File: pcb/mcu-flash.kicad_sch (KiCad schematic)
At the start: 25 parts, among them J1 Programming Header, SW1 SW_Push, U1 W25Q128JVS, U2 RP2040, Y1 ABM8AIG-12.000MHZ-12-2Z-T3

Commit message: Replaced through-hole components with SMD
- Other small edits (e.g. optional jumper to force USB-boot)
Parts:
- removed J1: Programming Header, symbol Connector_Generic:Conn_02x03_Odd_Even
- added J1: 0015910100, Connector_PinHeader_2.54mm:PinHeader_2x05_P2.54mm_Vertical_SMD, symbol Connector_Generic:Conn_02x05_Odd_Even
- added JP1: TSM-102-01-L-SV, Connector_PinHeader_2.54mm:PinHeader_1x02_P2.54mm_Vertical_SMD_Pin1Left, symbol Jumper:Jumper_2_Open
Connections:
- net +3.3V: now also J1.1 (Pin_1), J1.3 (Pin_3)
- net GND: now also J1.10 (Pin_10), J1.5 (Pin_5), J1.7 (Pin_7), J1.8 (Pin_8), J1.9 (Pin_9), JP1.1 (A)
- net QSPI_{CLK}: now also JP1.2 (B)
- net ~{RESET}: now also J1.6 (Pin_6)
- net at U2.25 (SWD): now also J1.4 (Pin_4)
- net at U2.24 (SWCLK): now also J1.2 (Pin_2)
- no-connect marks 15 -> 14
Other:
- company: (none) -> Open Ephys, Inc.
- title: (none) -> Open Ephys Commutator Controller

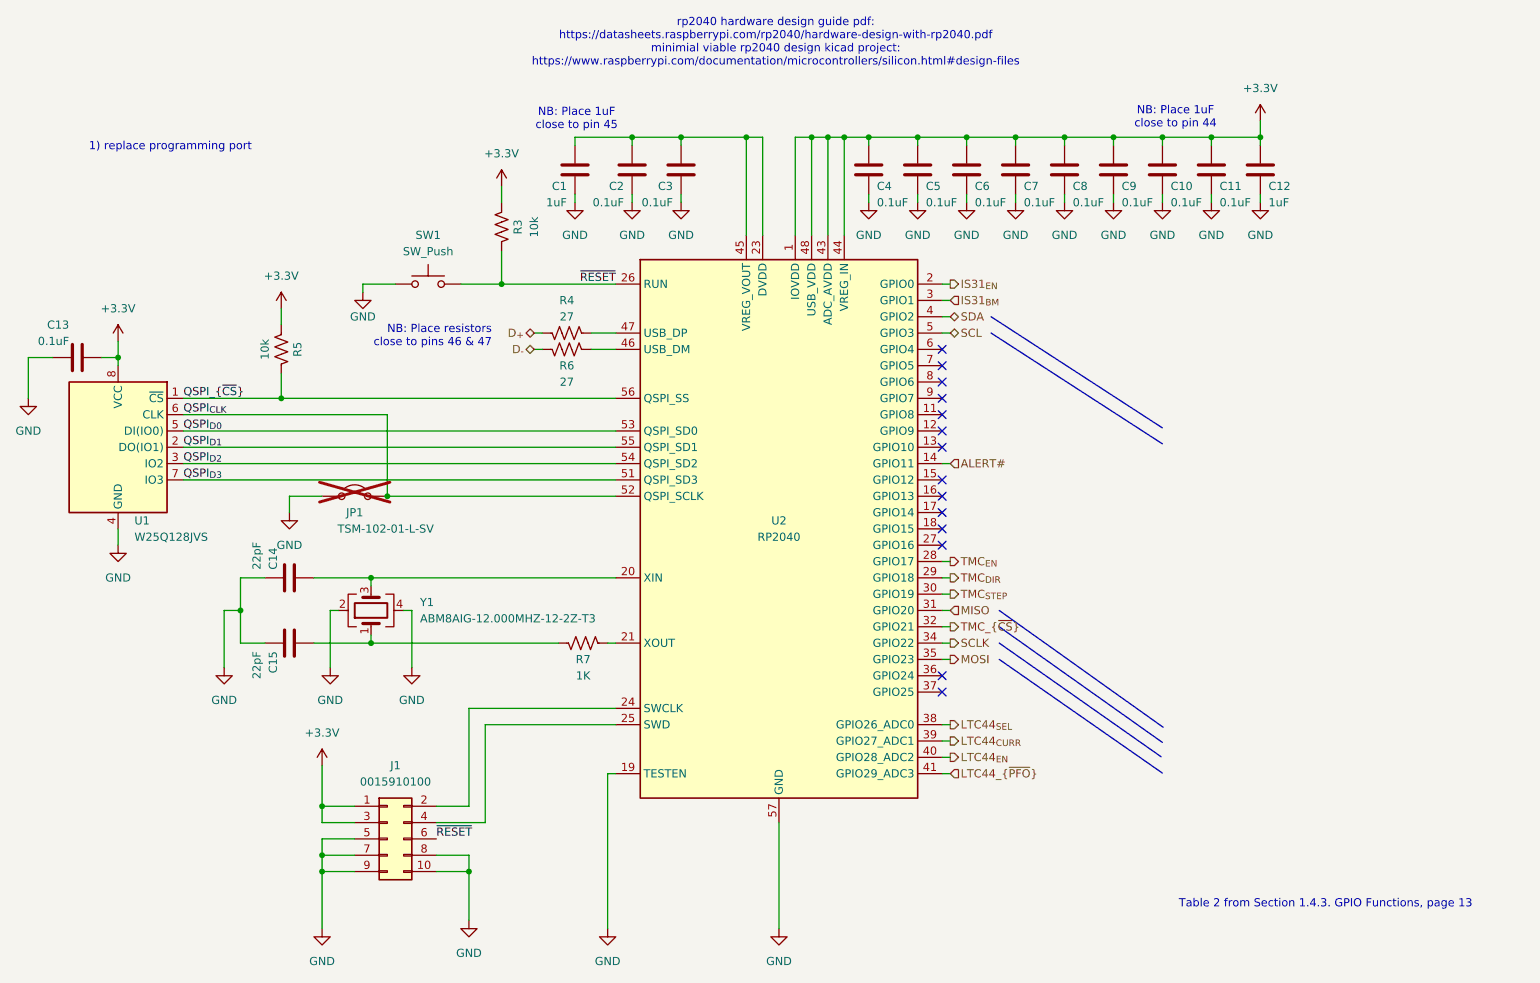
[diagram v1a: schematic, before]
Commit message: Add GPIO to programming header
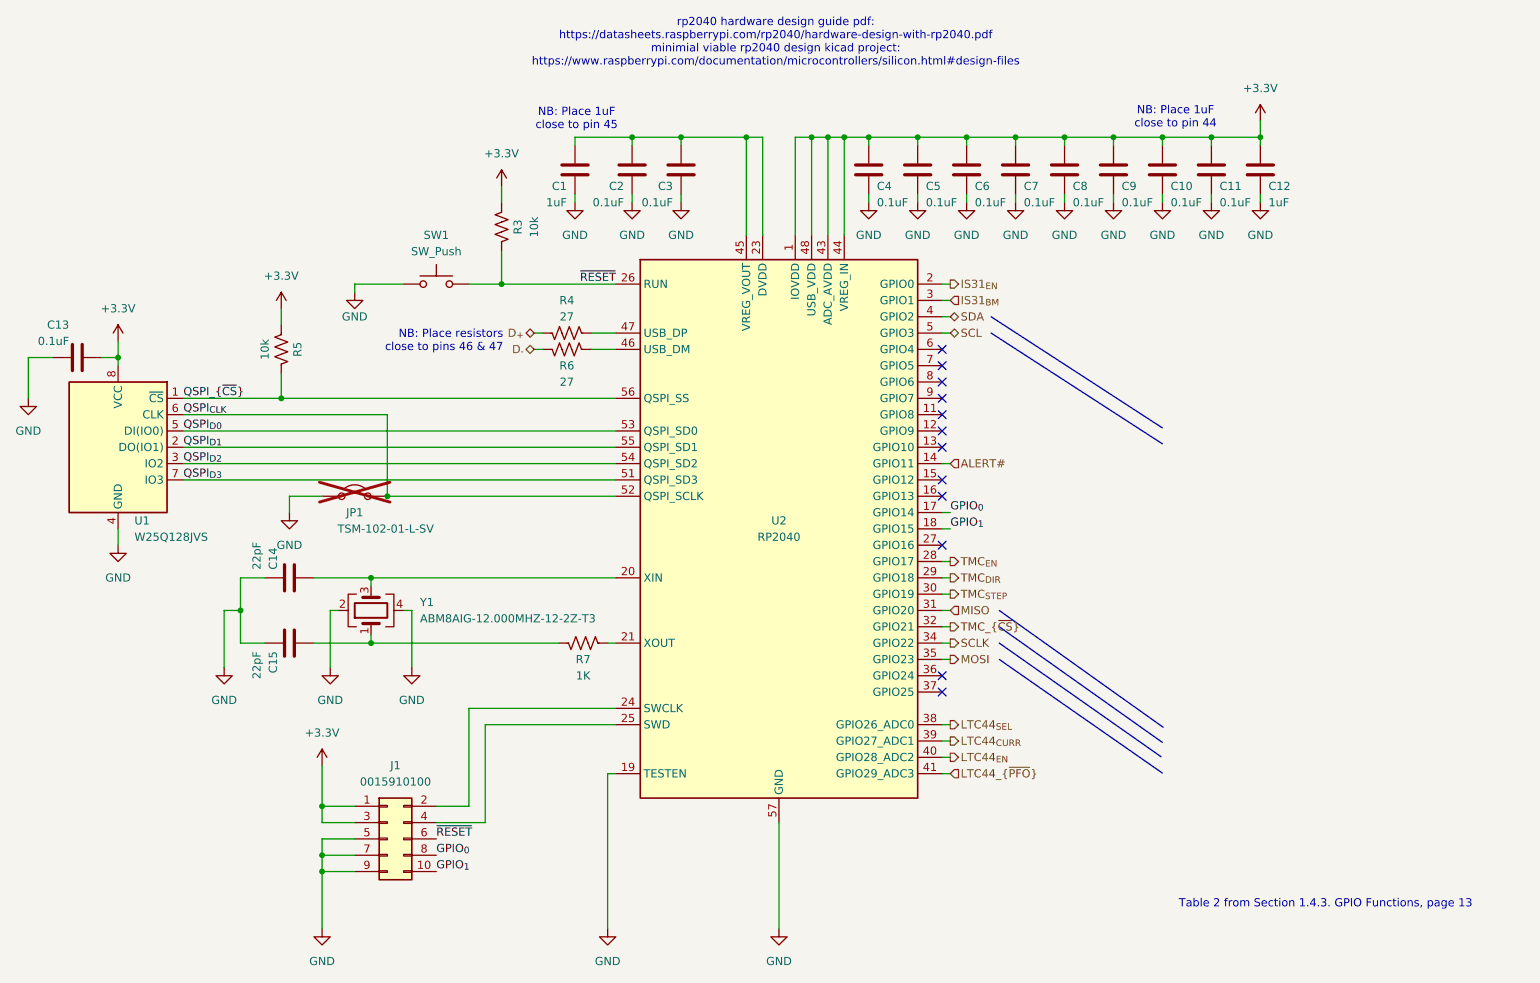
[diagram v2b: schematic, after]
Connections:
- net GND: no longer J1.10 (Pin_10), J1.8 (Pin_8)
- net GPIO_{0}: now reaches U2.17 (GPIO14)
- net GPIO_{0}: now also J1.8 (Pin_8)
- net GPIO_{1}: now reaches U2.18 (GPIO15)
- net GPIO_{1}: now also J1.10 (Pin_10)
- no-connect marks 14 -> 12
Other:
- note removed: "1) replace programming port"
- moved on the sheet: SW1
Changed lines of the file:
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@@
 	)
 	(junction
-		(at 93.98 154.94)
-		(diameter 0)
-		(color 0 0 0 0)
-	)
-	(junction
 		(at 152.4 40.64)
 		(diameter 0)
@@
 	)
 	(no_connect
-		(at 167.64 73.66)
+		(at 167.64 124.46)
 	)
 	(no_connect
-		(at 167.64 99.06)
+		(at 167.64 73.66)
 	)
 	(no_connect
@@
 	)
 	(no_connect
-		(at 167.64 127)
+		(at 167.64 86.36)
 	)
 	(no_connect
-		(at 167.64 86.36)
+		(at 167.64 127)
 	)
 	(no_connect
@@
 	)
 	(no_connect
-		(at 167.64 101.6)
-	)
-	(no_connect
 		(at 167.64 76.2)
 	)
@@
 	)
 	(no_connect
-		(at 167.64 124.46)
-	)
-	(no_connect
 		(at 167.64 83.82)
 	)
@@
 	(wire
 		(pts
+			(xy 168.91 99.06) (xy 167.64 99.06)
+		)
+		(stroke
+			(width 0)
+			(type default)
+		)
+	)
+	(wire
+		(pts
 			(xy 209.55 41.91) (xy 209.55 40.64)
 		)
@@
 	(wire
 		(pts
-			(xy 93.98 152.4) (xy 88.9 152.4)
-		)
-		(stroke
-			(width 0)
-			(type default)
-		)
-	)
-	(wire
-		(pts
 			(xy 168.91 119.38) (xy 167.64 119.38)
 		)
@@
 	(wire
 		(pts
-			(xy 88.9 154.94) (xy 93.98 154.94)
-		)
-		(stroke
-			(width 0)
-			(type default)
-		)
-	)
-	(wire
-		(pts
 			(xy 49.53 88.9) (xy 116.84 88.9)
 		)
@@
 	(wire
 		(pts
-			(xy 92.71 63.5) (xy 99.06 63.5)
+			(xy 93.98 63.5) (xy 99.06 63.5)
 		)
 		(stroke
@@
 	(wire
 		(pts
-			(xy 77.47 63.5) (xy 77.47 64.77)
+			(xy 76.2 63.5) (xy 76.2 64.77)
 		)
 		(stroke
@@
 	(wire
 		(pts
-			(xy 93.98 154.94) (xy 93.98 162.56)
-		)
-		(stroke
-			(width 0)
-			(type default)
-		)
-	)
-	(wire
-		(pts
 			(xy 147.32 40.64) (xy 147.32 55.88)
 		)
@@
 	(wire
 		(pts
-			(xy 93.98 152.4) (xy 93.98 154.94)
-		)
-		(stroke
-			(width 0)
-			(type default)
-		)
-	)
-	(wire
-		(pts
 			(xy 163.83 40.64) (xy 171.45 40.64)
 		)
@@
 	(wire
 		(pts
-			(xy 77.47 63.5) (xy 82.55 63.5)
+			(xy 76.2 63.5) (xy 83.82 63.5)
 		)
 		(stroke
@@
 	(wire
 		(pts
+			(xy 168.91 101.6) (xy 167.64 101.6)
+		)
+		(stroke
+			(width 0)
+			(type default)
+		)
+	)
+	(wire
+		(pts
 			(xy 163.83 41.91) (xy 163.83 40.64)
 		)
@@
 	(text "NB: Place resistors\nclose to pins 46 & 47"
 		(exclude_from_sim no)
-		(at 97.536 73.406 0)
+		(at 99.314 74.168 0)
 		(effects
 			(font
@@
 		)
 	)
-	(text "1) replace programming port\n"
-		(exclude_from_sim no)
-		(at 47.498 42.164 0)
-		(effects
-			(font
-				(size 1.27 1.27)
-			)
-		)
-	)
 	(text "Table 2 from Section 1.4.3. GPIO Functions, page 13"
 		(exclude_from_sim no)
@@
 		)
 	)
+	(label "GPIO_{0}"
+		(at 168.91 99.06 0)
+		(fields_autoplaced yes)
+		(effects
+			(font
+				(size 1.27 1.27)
+			)
+			(justify left bottom)
+		)
+	)
 	(label "QSPI_{D3}"
 		(at 49.53 93.98 0)
@@
 		)
 	)
+	(label "GPIO_{1}"
+		(at 88.9 154.94 0)
+		(fields_autoplaced yes)
+		(effects
+			(font
+				(size 1.27 1.27)
+			)
+			(justify left bottom)
+		)
+	)
+	(label "GPIO_{1}"
+		(at 168.91 101.6 0)
+		(fields_autoplaced yes)
+		(effects
+			(font
+				(size 1.27 1.27)
+			)
+			(justify left bottom)
+		)
+	)
+	(label "GPIO_{0}"
+		(at 88.9 152.4 0)
+		(fields_autoplaced yes)
+		(effects
+			(font
+				(size 1.27 1.27)
+			)
+			(justify left bottom)
+		)
+	)
 	(label "QSPI_{~{CS}}"
 		(at 49.53 81.28 0)
@@
 	(symbol
 		(lib_id "power:GND")
-		(at 77.47 64.77 0)
+		(at 76.2 64.77 0)
 		(unit 1)
 		(exclude_from_sim no)
@@
 		(dnp no)
 		(property "Reference" "#PWR016"
-			(at 77.47 71.12 0)
+			(at 76.2 71.12 0)
 			(effects
 				(font
@@
 		)
 		(property "Value" "GND"
-			(at 77.47 68.58 0)
+			(at 76.2 68.58 0)
 			(effects
 				(font
@@
 		)
 		(property "Footprint" ""
-			(at 77.47 64.77 0)
+			(at 76.2 64.77 0)
 			(effects
 				(font
@@
 		)
 		(property "Datasheet" ""
-			(at 77.47 64.77 0)
+			(at 76.2 64.77 0)
 			(effects
 				(font
@@
 		)
 		(property "Description" "Power symbol creates a global label with name \"GND\" , ground"
-			(at 77.47 64.77 0)
+			(at 76.2 64.77 0)
 			(effects
 				(font
@@
 	(symbol
 		(lib_id "power:GND")
-		(at 93.98 162.56 0)
-		(mirror y)
-		(unit 1)
-		(exclude_from_sim no)
-		(in_bom yes)
-		(on_board yes)
-		(dnp no)
-		(fields_autoplaced yes)
-		(property "Reference" "#PWR077"
-			(at 93.98 168.91 0)
-			(effects
-				(font
-					(size 1.27 1.27)
-				)
-				(hide yes)
-			)
-		)
-		(property "Value" "GND"
-			(at 93.98 167.64 0)
-			(effects
-				(font
-					(size 1.27 1.27)
-				)
-			)
-		)
-		(property "Footprint" ""
-			(at 93.98 162.56 0)
-			(effects
-				(font
-					(size 1.27 1.27)
-				)
-				(hide yes)
-			)
-		)
-		(property "Datasheet" ""
-			(at 93.98 162.56 0)
-			(effects
-				(font
-					(size 1.27 1.27)
-				)
-				(hide yes)
-			)
-		)
-		(property "Description" "Power symbol creates a global label with name \"GND\" , ground"
-			(at 93.98 162.56 0)
-			(effects
-				(font
-					(size 1.27 1.27)
-				)
-				(hide yes)
-			)
-		)
-		(pin "1"
-		)
-		(instances
-			(project "oe-commutator-controller"
-				(path "/f8e1d654-dc44-4fb2-953c-f5982945ff40/f332ab09-c494-4f8f-98bf-7facb28de9af"
-					(reference "#PWR077")
-					(unit 1)
-				)
-			)
-		)
-	)
-	(symbol
-		(lib_id "power:GND")
 		(at 115.57 163.83 0)
 		(mirror y)
@@
 		)
 		(instances
-			(project ""
+			(project "oe-commutator-controller"
 				(path "/f8e1d654-dc44-4fb2-953c-f5982945ff40/f332ab09-c494-4f8f-98bf-7facb28de9af"
 					(reference "JP1")
@@
 		)
 		(instances
-			(project ""
+			(project "oe-commutator-controller"
 				(path "/f8e1d654-dc44-4fb2-953c-f5982945ff40/f332ab09-c494-4f8f-98bf-7facb28de9af"
 					(reference "J1")
@@
 	(symbol
 		(lib_id "Switch:SW_Push")
-		(at 87.63 63.5 0)
+		(at 88.9 63.5 0)
 		(unit 1)
 		(exclude_from_sim no)
@@
 		(fields_autoplaced yes)
 		(property "Reference" "SW1"
-			(at 87.63 55.88 0)
+			(at 88.9 55.88 0)
 			(effects
 				(font
@@
 		)
 		(property "Value" "SW_Push"
-			(at 87.63 58.42 0)
+			(at 88.9 58.42 0)
 			(effects
 				(font
@@
 		)
 		(property "Footprint" "Button_Switch_SMD:SW_Push_1P1T_NO_CK_KMR2"
-			(at 87.63 58.42 0)
+			(at 88.9 58.42 0)
 			(effects
 				(font
@@
 		)
 		(property "Datasheet" "https://www.ckswitches.com/media/1479/kmr2.pdf"
-			(at 87.63 58.42 0)
+			(at 88.9 58.42 0)
 			(effects
 				(font
@@
 		)
 		(property "Description" "Push button switch, generic, two pins"
-			(at 87.63 63.5 0)
+			(at 88.9 63.5 0)
 			(effects
 				(font

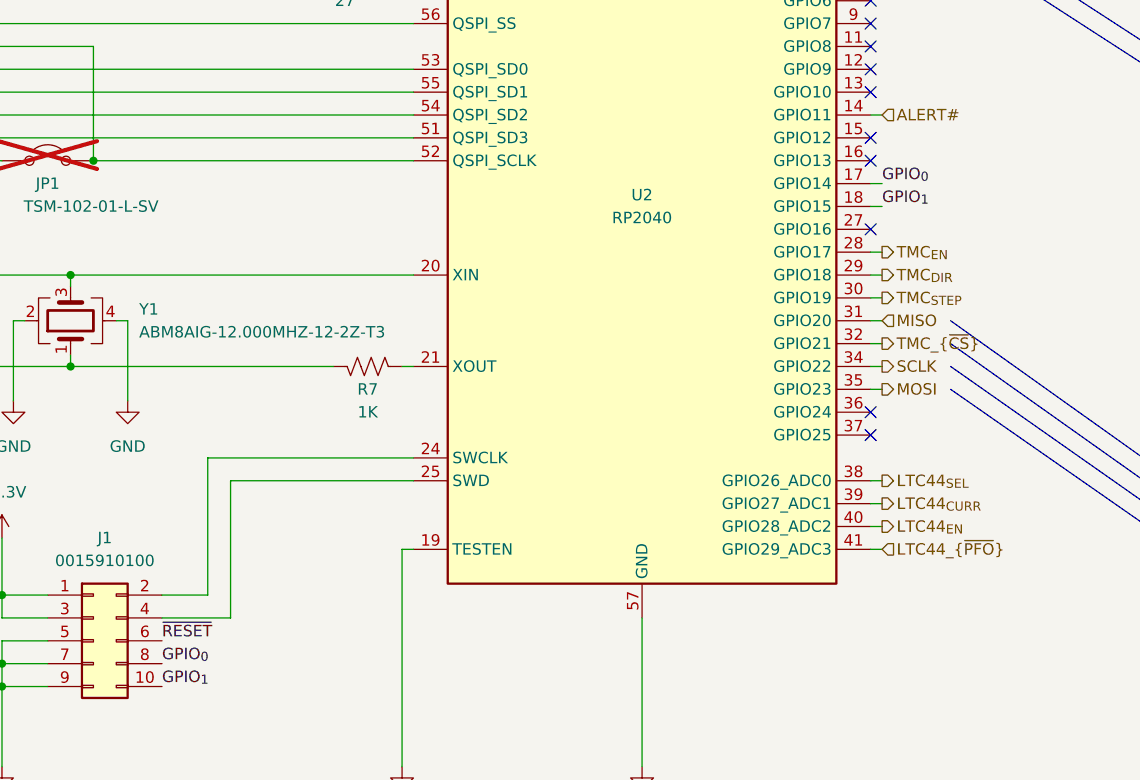
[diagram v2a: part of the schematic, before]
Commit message: Rev D PCB WIP for Review
- Before going into further minutiae, get review
- Components are laid out and routed
- Fails DRC check, requires vias for better GND plane, there are traces
  in the outer keepout zone, remove S5?
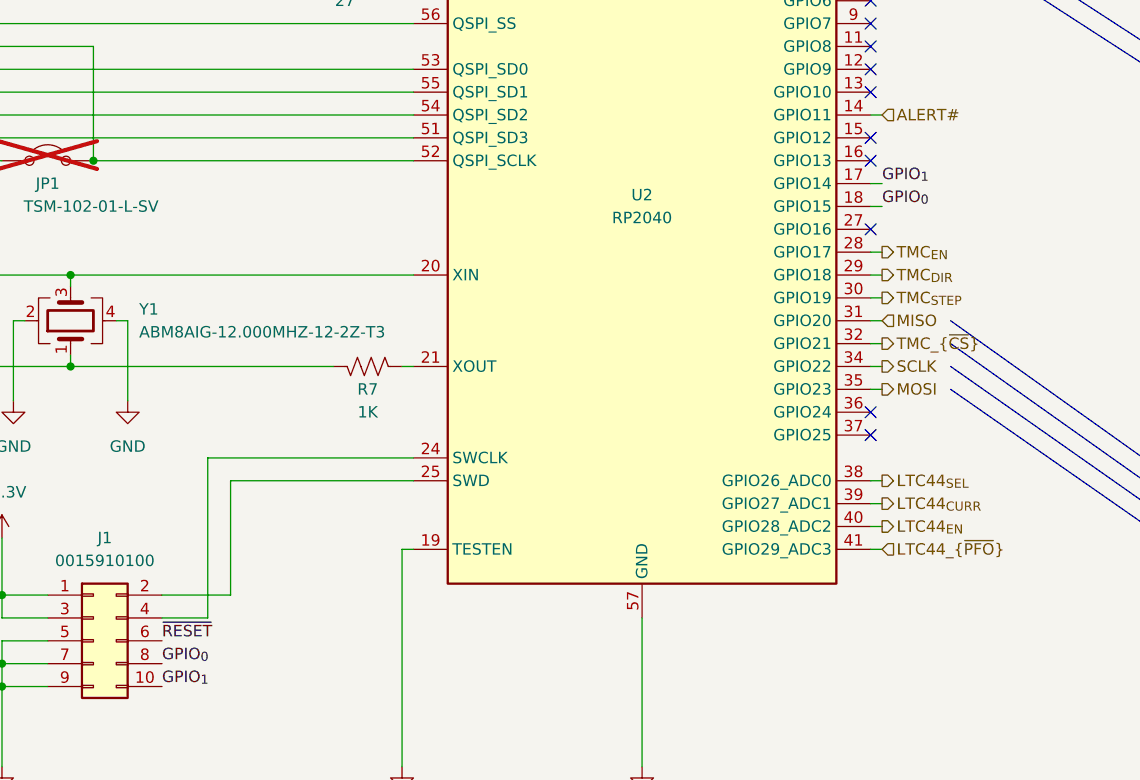
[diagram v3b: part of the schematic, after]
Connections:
- net GPIO_{0}: now also U2.18 (GPIO15); no longer U2.17 (GPIO14)
- net GPIO_{1}: now also U2.17 (GPIO14); no longer U2.18 (GPIO15)
- net at U2.24 (SWCLK): now also J1.4 (Pin_4); no longer J1.2 (Pin_2)
- net at U2.25 (SWD): now also J1.2 (Pin_2); no longer J1.4 (Pin_4)
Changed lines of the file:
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@@
 	(wire
 		(pts
-			(xy 88.9 144.78) (xy 93.98 144.78)
-		)
-		(stroke
-			(width 0)
-			(type default)
-		)
-	)
-	(wire
-		(pts
 			(xy 163.83 49.53) (xy 163.83 50.8)
 		)
@@
 	(wire
 		(pts
+			(xy 93.98 147.32) (xy 93.98 129.54)
+		)
+		(stroke
+			(width 0)
+			(type default)
+		)
+	)
+	(wire
+		(pts
 			(xy 39.37 72.39) (xy 39.37 74.93)
 		)
@@
 	(wire
 		(pts
-			(xy 96.52 132.08) (xy 96.52 147.32)
+			(xy 96.52 132.08) (xy 96.52 144.78)
 		)
 		(stroke
@@
 	(wire
 		(pts
+			(xy 88.9 144.78) (xy 96.52 144.78)
+		)
+		(stroke
+			(width 0)
+			(type default)
+		)
+	)
+	(wire
+		(pts
 			(xy 105.41 71.12) (xy 104.14 71.12)
 		)
@@
 	(wire
 		(pts
+			(xy 88.9 147.32) (xy 93.98 147.32)
+		)
+		(stroke
+			(width 0)
+			(type default)
+		)
+	)
+	(wire
+		(pts
 			(xy 168.91 116.84) (xy 167.64 116.84)
 		)
@@
 	(wire
 		(pts
-			(xy 93.98 144.78) (xy 93.98 129.54)
-		)
-		(stroke
-			(width 0)
-			(type default)
-		)
-	)
-	(wire
-		(pts
-			(xy 96.52 147.32) (xy 88.9 147.32)
-		)
-		(stroke
-			(width 0)
-			(type default)
-		)
-	)
-	(wire
-		(pts
 			(xy 115.57 119.38) (xy 116.84 119.38)
 		)
@@
 		)
 	)
-	(label "QSPI_{D1}"
-		(at 49.53 88.9 0)
+	(label "GPIO_{0}"
+		(at 168.91 101.6 0)
 		(fields_autoplaced yes)
 		(effects
@@
 		)
 	)
-	(label "GPIO_{0}"
-		(at 168.91 99.06 0)
+	(label "QSPI_{D1}"
+		(at 49.53 88.9 0)
 		(fields_autoplaced yes)
 		(effects
@@
 		)
 	)
-	(label "~{RESET}"
-		(at 116.84 63.5 180)
+	(label "GPIO_{1}"
+		(at 168.91 99.06 0)
 		(fields_autoplaced yes)
 		(effects
@@
 				(size 1.27 1.27)
 			)
-			(justify right bottom)
+			(justify left bottom)
 		)
 	)
-	(label "GPIO_{1}"
-		(at 88.9 154.94 0)
+	(label "~{RESET}"
+		(at 116.84 63.5 180)
 		(fields_autoplaced yes)
 		(effects
@@
 				(size 1.27 1.27)
 			)
-			(justify left bottom)
+			(justify right bottom)
 		)
 	)
 	(label "GPIO_{1}"
-		(at 168.91 101.6 0)
+		(at 88.9 154.94 0)
 		(fields_autoplaced yes)
 		(effects
